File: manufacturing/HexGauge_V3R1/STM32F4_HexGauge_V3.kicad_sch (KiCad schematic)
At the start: 0 parts

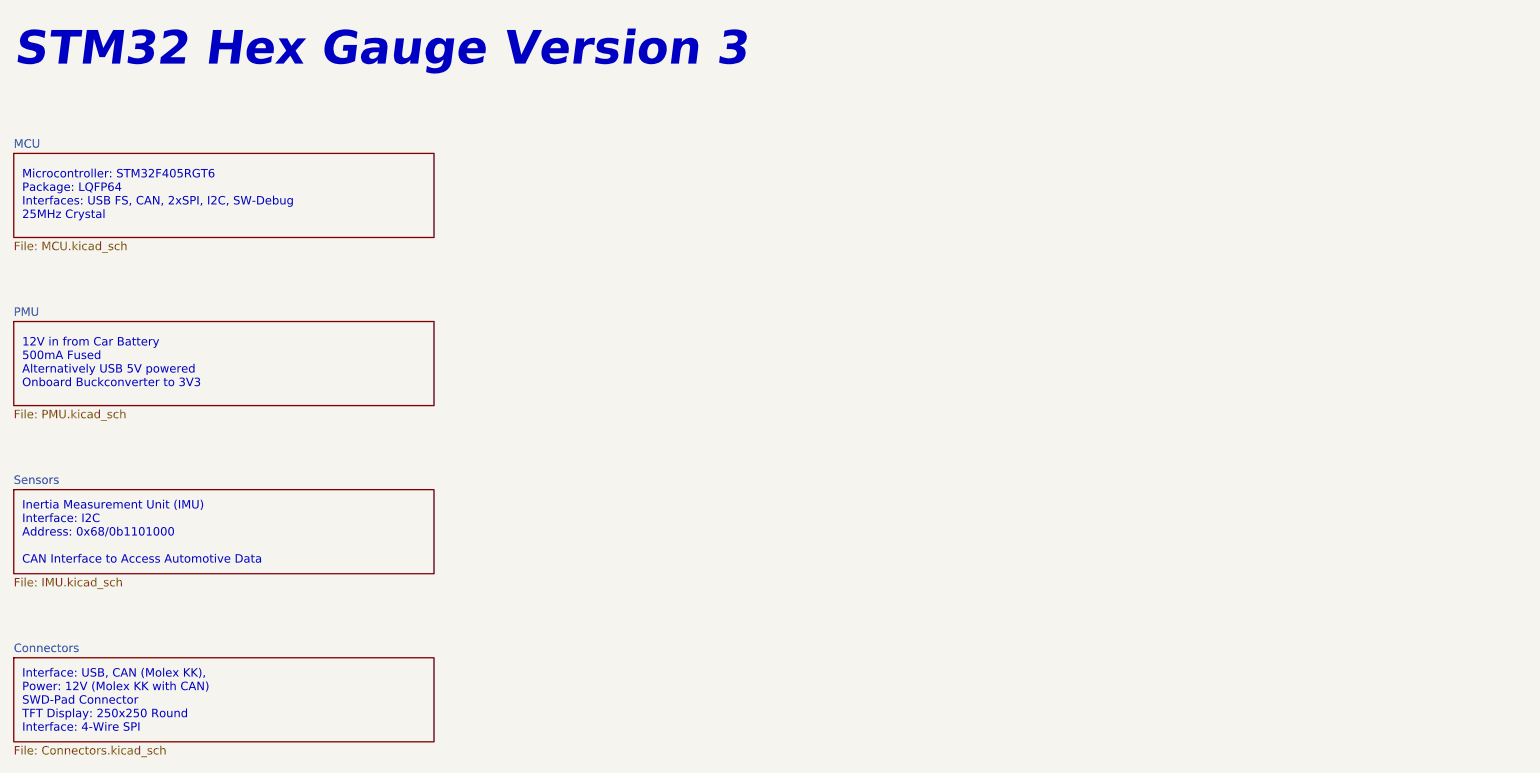
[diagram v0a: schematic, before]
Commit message: Cleaned Up Schematic
Added Blockdiagram
Reannotated Symbols
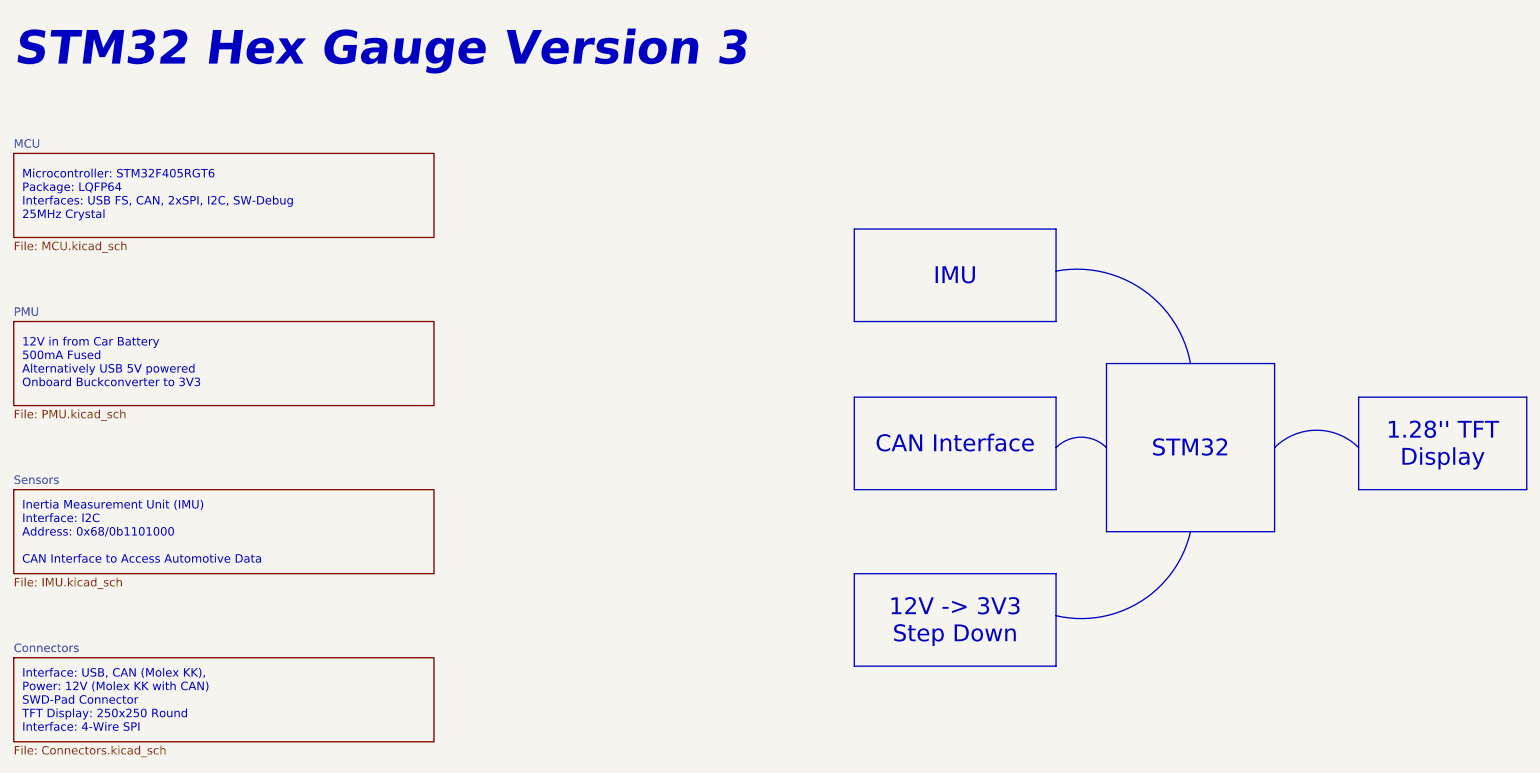
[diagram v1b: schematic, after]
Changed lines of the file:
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@@
     (comment 1 "Multipurpose Automotive Gauge")
+  )
+  (arc (start 215.9 82.55) (mid 222.25 79.9198) (end 228.6 82.55)
+    (stroke (width 0) (type default))
+    (fill (type none))
+  )
+  (arc (start 182.88 82.55) (mid 186.69 80.9719) (end 190.5 82.55)
+    (stroke (width 0) (type default))
+    (fill (type none))
+  )
+  (arc (start 203.2 95.25) (mid 195.6703 105.8084) (end 182.88 107.95)
+    (stroke (width 0) (type default))
+    (fill (type none))
+  )
+  (arc (start 182.88 55.88) (mid 195.9333 58.6566) (end 203.2 69.85)
+    (stroke (width 0) (type default))
+    (fill (type none))
+  )
+  (text_box "IMU"
+    (at 152.4 49.53 0) (size 30.48 13.97)
+    (stroke (width 0) (type default))
+    (fill (type none))
+    (effects (font (size 2.54 2.54)))
+  )
+  (text_box "1.28'' TFT\nDisplay\n"
+    (at 228.6 74.93 0) (size 25.4 13.97)
+    (stroke (width 0) (type default))
+    (fill (type none))
+    (effects (font (size 2.54 2.54)))
+  )
+  (text_box "CAN Interface"
+    (at 152.4 74.93 0) (size 30.48 13.97)
+    (stroke (width 0) (type default))
+    (fill (type none))
+    (effects (font (size 2.54 2.54)))
+  )
+  (text_box "12V -> 3V3\nStep Down"
+    (at 152.4 101.6 0) (size 30.48 13.97)
+    (stroke (width 0) (type default))
+    (fill (type none))
+    (effects (font (size 2.54 2.54)))
+  )
+  (text_box "STM32"
+    (at 190.5 69.85 0) (size 25.4 25.4)
+    (stroke (width 0) (type default))
+    (fill (type color) (color 0 0 0 0))
+    (effects (font (size 2.54 2.54)))
   )
   (text "Interface: USB, CAN (Molex KK), \nPower: 12V (Molex KK with CAN)\nSWD-Pad Connector\nTFT Display: 250x250 Round\nInterface: 4-Wire SPI"
